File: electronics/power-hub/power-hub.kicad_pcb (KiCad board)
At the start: 4 copper layers, 76 x 140 mm, 158 parts, among them J1 PD IN, J2 ROW A, J3 ROW B, J4 ROW C, J5 ROW D, J6 USB, Q1 IRF7842TRPBF, Q2 IRF7842TRPBF, SW1 RESET, SW2 BOOT, U1 AP33772SDKZ-13-FA02, U11 TPS26600PWPR, U12 TPS26600PWPR, U13 TPS26600PWPR, U14 TPS26600PWPR, U2 LMR51635YDDCR, U3 AP2112K-3.3TRG1, U4 ESP32-S3-MINI-1-N8, U5 USBLC6-2SC6, U6 TCAN1462V

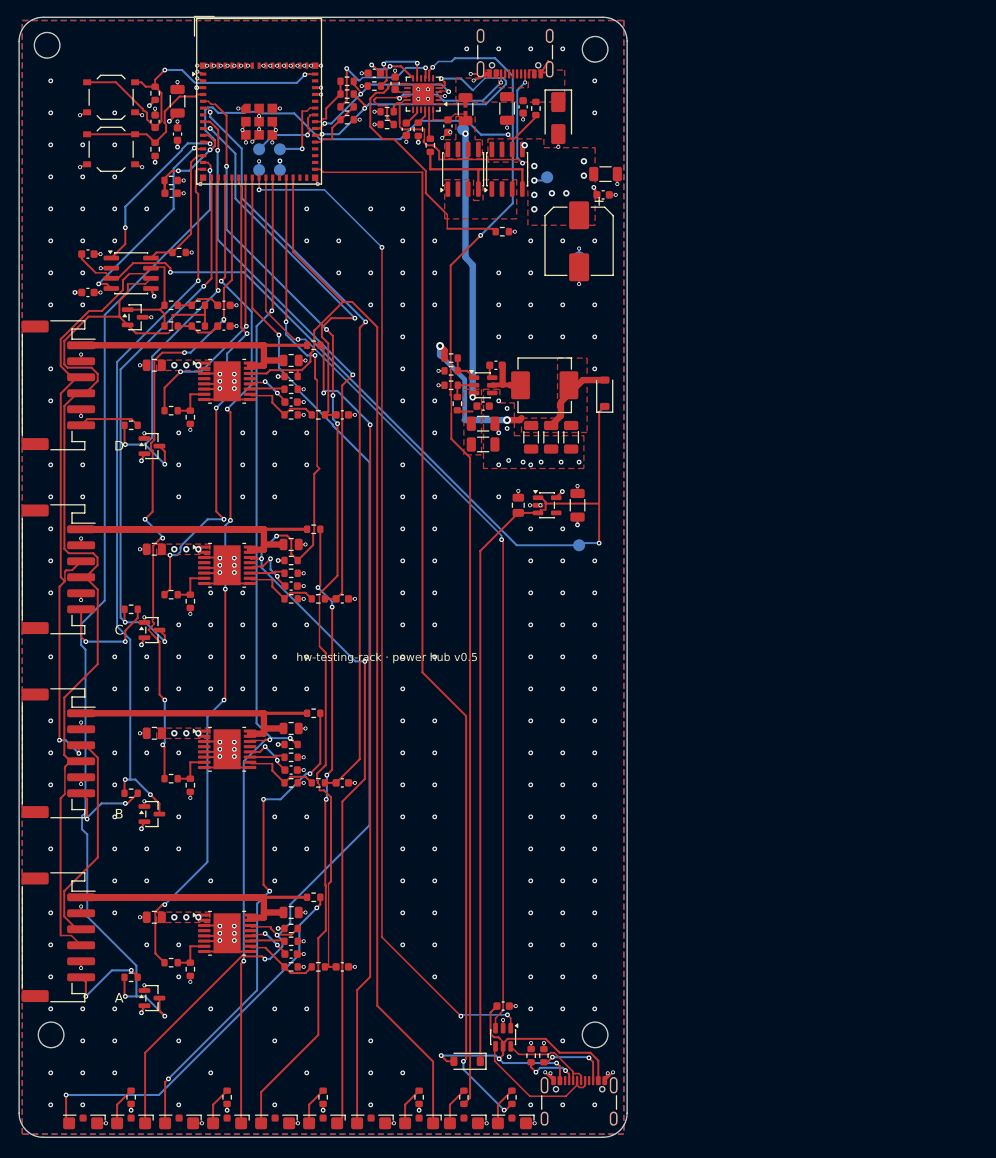
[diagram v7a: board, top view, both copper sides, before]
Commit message: Hub row outputs with the OUT pinout: one row cable for everything
The user chose to mirror the hub's row outputs too (option a'): J2-J5 now
carry the bay nodes' OUT pinout (1 POS, 2 GND, 3 CAN_L, 4 CAN_H, 5 GND,
6 VRACK).  Every link runs from an output to an input, so every row cable,
feed or jumper, is the same: pin n to pin 7-n, both plugs the same face up.
The feeds take a half turn along their 25-60 cm; the CAN pair stays
together between its GND pins.

Hub: each ROW track leaves its eFuse as before, stops short of the
connector's rear pin, drops to B.Cu beside the connector (three vias) and
comes back up at pin 6, keeping the top side free for the CAN pair; R10x
sits behind pin 1.  The AP33772S's I2C routes from the first layout are
fixed in design.py (one re-route left PD_SDA without a way out), and the
pre-drawn CC2 stub goes (the router leaves CC2 behind the receptacle).

Re-routed: ERC 0, DRC 0 errors, unconnected 0, parity 0; CAN pair to the
rows 18-102 mm (within ±5 mm of before), H-L 4.2-8.3 mm (was 4.6-10.4),
same coupling; 146 3D models, 0 stand-ins.  docs/can.md (the contract),
cabling.md, electronics.md, the Konnect review, the BOM feed line and the
hub's POS comment follow.

Co-Authored-By: Claude Opus 5.5 <noreply@anthropic.com>
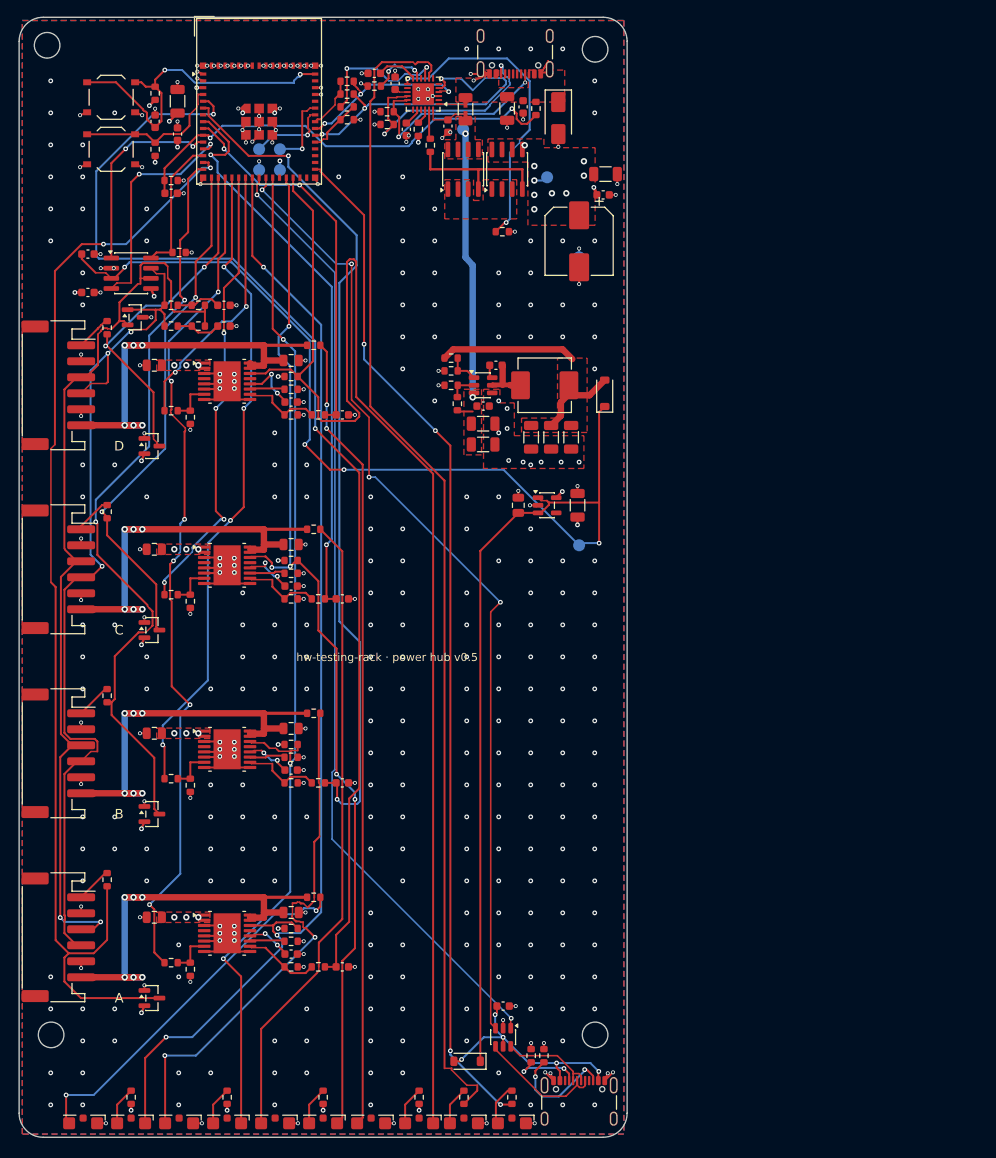
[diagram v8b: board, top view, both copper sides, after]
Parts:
- moved R101 12.6 mm to (11.0, 107.8), turned to 90 degrees
- moved R102 12.6 mm to (11.0, 84.8), turned to 90 degrees
- moved R103 12.6 mm to (11.0, 61.8), turned to 90 degrees
- moved R104 12.6 mm to (11.0, 38.8), turned to 90 degrees
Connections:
- J2 pad 1: /Outputs/ROW_A -> /Outputs/POS_A_CONN
- J2 pad 3: CAN_H -> CAN_L
- J2 pad 4: CAN_L -> CAN_H
- J2 pad 6: /Outputs/POS_A_CONN -> /Outputs/ROW_A
- J3 pad 1: /Outputs/ROW_B -> /Outputs/POS_B_CONN
- J3 pad 3: CAN_H -> CAN_L
- J3 pad 4: CAN_L -> CAN_H
- J3 pad 6: /Outputs/POS_B_CONN -> /Outputs/ROW_B
- J4 pad 1: /Outputs/ROW_C -> /Outputs/POS_C_CONN
- J4 pad 3: CAN_H -> CAN_L
- J4 pad 4: CAN_L -> CAN_H
- J4 pad 6: /Outputs/POS_C_CONN -> /Outputs/ROW_C
- J5 pad 1: /Outputs/ROW_D -> /Outputs/POS_D_CONN
- J5 pad 3: CAN_H -> CAN_L
- J5 pad 4: CAN_L -> CAN_H
- J5 pad 6: /Outputs/POS_D_CONN -> /Outputs/ROW_D
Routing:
- net FLT_D: track 144.2 -> 178.0 mm
- net ADC_IMON_A: track 120.1 -> 145.6 mm, vias 4 -> 2
- net /Outputs/ROW_D: track 35.6 -> 54.5 mm, vias 0 -> 6
- net /Outputs/ROW_B: track 35.6 -> 54.4 mm, vias 0 -> 6
- net POS_A: track 125.9 -> 141.3 mm, vias 3 -> 2
- net /Controller/USB_VBUS: track 42.9 -> 30.2 mm, vias 3 -> 5
- net ADC_IMON_B: track 96.1 -> 106.6 mm
- net /Input/PD_CC1: track 36.4 -> 26.3 mm
- net /Outputs/POS_C_CONN: track 13.9 -> 4.73 mm, vias 2 -> 0
- net VBUS_SENSE: track 66.1 -> 57.2 mm, vias 3 -> 2
- net +5V: track 182.4 -> 190.8 mm, vias 2 -> 4
- net /Controller/CTL_LED: track 136.6 -> 128.4 mm, vias 2 -> 4
- net FLT_C: track 139.5 -> 131.4 mm
- net /Controller/USB_DN: track 127.8 -> 119.9 mm, vias 4 -> 2
- net /Outputs/POS_B_CONN: track 11.5 -> 4.50 mm, vias 2 -> 0
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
